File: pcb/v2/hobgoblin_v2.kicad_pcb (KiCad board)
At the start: 2 copper layers, 47 parts, among them J1 5V, J2 RC2014EXT1, J3 RC2014EXT2, SW1 RESET, SW2 ROMBNK, SW3 USBUART, U1 74LS32, U10 MC68B50, U2 74LS14, U3 Z80CPU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

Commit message: Start using GALs in V2
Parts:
- added REF**: M3, MountingHole:MountingHole_3.2mm_M3, F.Cu at (186.5, 33.5)
- added REF**: M3, MountingHole:MountingHole_3.2mm_M3, F.Cu at (33.5, 141.5)
- added REF**: M3, MountingHole:MountingHole_3.2mm_M3, F.Cu at (33.5, 33.5)
- added REF**: M3, MountingHole:MountingHole_3.2mm_M3, F.Cu at (186.5, 141.5)
- moved C10 168.4 mm to (269.3, 133.6)
- moved R10 168.4 mm to (256.0, 129.6)
- moved R5 168.4 mm to (256.0, 137.7)
- moved C11 168.4 mm to (286.4, 115.4)
- moved C7 168.4 mm to (256.0, 141.8)
- moved D1 168.4 mm to (280.8, 111.6)
- moved R11 168.4 mm to (256.0, 133.6)
- moved R2 168.4 mm to (273.0, 121.0)
- moved R4 168.4 mm to (292.5, 103.0)
- moved R8 168.4 mm to (292.5, 99.0)
- moved R9 168.4 mm to (273.0, 116.9)
- moved SW1 168.4 mm to (273.5, 125.0)
- moved U1 168.4 mm to (233.2, 136.4)
- moved U7 168.4 mm to (244.8, 126.6)
- moved U9 168.4 mm to (281.3, 84.8)
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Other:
- board outline added: 160 x 115 mm

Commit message: Draft component placement
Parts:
- added C14: 10uF, Capacitor_THT:CP_Radial_D4.0mm_P1.50mm, F.Cu at (101.2, 37.1)
- added C15: 0.1uF, Capacitor_THT:C_Disc_D3.8mm_W2.6mm_P2.50mm, F.Cu at (117.8, 39.8)
- added C16: 0.1uF, Capacitor_THT:C_Disc_D3.8mm_W2.6mm_P2.50mm, F.Cu at (41.8, 81.2)
- added J4: MINIUSB, Connector_USB:USB_Mini-B_Lumberg_2486_01_Horizontal, F.Cu at (162.2, 34.6)
- added JP1: USB_VCC, Connector_PinSocket_2.54mm:PinSocket_1x02_P2.54mm_Vertical, F.Cu at (163.7, 43.4)
- U4: value 74LS138 -> GAL16V8/IO; footprint Package_DIP:DIP-16_W7.62mm_LongPads -> Package_DIP:DIP-20_W7.62mm_Socket_LongPads
- U5: value 74LS32 -> FT232RL; footprint Package_DIP:DIP-14_W7.62mm_LongPads -> Package_SO:SSOP-28_5.3x10.2mm_P0.65mm
- U9: value GAL16V8 -> GAL16V8/MEM
- moved C8 211.1 mm to (56.8, 81.2), turned to 90 degrees
- moved D1 207.6 mm to (73.2, 109.5), turned to 180 degrees
- moved C1 206.0 mm to (60.5, 115.2)
- moved C13 195.0 mm to (68.0, 119.4)
- moved C3 188.0 mm to (66.9, 78.2), turned to 90 degrees
- moved R4 185.0 mm to (107.6, 101.5), turned to 180 degrees
- moved SW3 178.0 mm to (126.7, 43.6), turned to 90 degrees
- moved U2 177.6 mm to (65.4, 122.5)
- moved C4 169.7 mm to (84.5, 119.4)
- moved R8 161.9 mm to (130.7, 97.0)
- moved R3 160.0 mm to (81.1, 108.0)
- moved SW1 159.4 mm to (141.5, 35.8)
- moved R1 157.0 mm to (91.2, 111.2), turned to 180 degrees
- moved C2 154.4 mm to (106.3, 49.8)
- moved C5 152.9 mm to (101.0, 119.4)
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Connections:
- CF1 pad 7: /~{PORT10} -> /~{IO_CF}
- SW3 pad 4: /RX -> /USB_UART/RX
- SW3 pad 5: /~{RTS}_1 -> /USB_UART/~{RTS}
- SW3 pad 6: /TX -> /USB_UART/TX
- U10 pad 10: /A7 -> unconnected-(U10-Pad10)
- U10 pad 8: /~{M1} -> unconnected-(U10-Pad8)
- U10 pad 9: /A6 -> /~{IO_UART}
- U4 pad 1: /A3 -> /~{M1}
- U4 pad 10: unconnected-(U4-Pad10) -> GND
- U4 pad 11: unconnected-(U4-Pad11) -> /A10
- U4 pad 12: unconnected-(U4-Pad12) -> /A15
- U4 pad 13: /~{PORT10} -> /A14
- U4 pad 14: unconnected-(U4-Pad14) -> /~{ROM_OFF}
- U4 pad 15: unconnected-(U4-Pad15) -> /~{IO_CF}
- U4 pad 16: VCC -> /~{IO_UART}
- U4 pad 2: /A4 -> /~{IOWR}
- U4 pad 3: /A5 -> /A3
- U4 pad 4: /A7 -> /A4
- U4 pad 5: /A6 -> /A5
- U4 pad 6: /~{M1} -> /A6
- U4 pad 7: /~{PORT38} -> /A7
- U4 pad 8: GND -> /A8
- U4 pad 9: unconnected-(U4-Pad9) -> /A9
- U5 pad 1: /~{IOWR} -> /USB_UART/RX
- U5 pad 10: (no net) -> unconnected-(U5-Pad10)
- U5 pad 11: (no net) -> /USB_UART/~{RTS}
- U5 pad 12: (no net) -> unconnected-(U5-Pad12)
- U5 pad 13: (no net) -> unconnected-(U5-Pad13)
- U5 pad 14: VCC -> unconnected-(U5-Pad14)
- U5 pad 2: /~{PORT38} -> unconnected-(U5-Pad2)
- U5 pad 3: /~{ROMOFF} -> unconnected-(U5-Pad3)
- U5 pad 4: (no net) -> VCC
- U5 pad 5: (no net) -> /USB_UART/TX
- U5 pad 6: (no net) -> unconnected-(U5-Pad6)
- U5 pad 9: (no net) -> unconnected-(U5-Pad9)
- U7 pad 5: /~{ROMOFF} -> /~{ROM_OFF}

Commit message: Realign components
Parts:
- moved X2 15.6 mm to (72.2, 33.8)
- moved X1 15.0 mm to (55.7, 33.8)
- moved JP1 14.4 mm to (152.5, 34.3)
- moved C11 14.1 mm to (124.5, 101.8)
- moved C3 14.1 mm to (56.9, 68.2)
- moved C1 14.1 mm to (50.5, 105.2)
- moved C10 14.1 mm to (156.3, 39.8)
- moved C13 14.1 mm to (58.0, 109.4)
- moved C2 14.1 mm to (96.3, 39.8)
- moved C4 14.1 mm to (74.5, 109.4)
- moved C5 14.1 mm to (91.0, 109.4)
- moved C6 14.1 mm to (126.3, 40.0)
- moved C7 14.1 mm to (108.0, 101.8)
- moved C8 14.1 mm to (46.8, 71.2)
- moved C9 14.1 mm to (139.0, 103.2)
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
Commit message: CF socket properties
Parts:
- CF1: value CF_Socket -> CompactFlash
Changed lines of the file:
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@@
     (property "Sheetname" "")
     (attr smd)
-    (fp_text reference "CF1" (at 7.22 0 90) (layer "F.SilkS")
+    (fp_text reference "CF1" (at 7.22 0 90) (layer "F.SilkS") hide
       (effects (font (size 1 1) (thickness 0.15)))
     )
-    (fp_text value "CF_Socket" (at 10.39 0 90) (layer "F.Fab")
+    (fp_text value "CompactFlash" (at 10.39 0 90) (layer "F.SilkS")
       (effects (font (size 1 1) (thickness 0.15)))
     )

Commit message: Tweak silkscreen
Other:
- board text added: "Hobgoblin Computer v2.0 Ilya Strukov 2022"
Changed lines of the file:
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@@
       (effects (font (size 1 1) (thickness 0.15)))
     )
-    (fp_text value "CompactFlash" (at 10.39 0 90) (layer "F.SilkS")
+    (fp_text value "CompactFlash" (at 18 0 90) (layer "F.SilkS")
       (effects (font (size 1 1) (thickness 0.15)))
     )
@@
   (gr_arc (start 180 133) (mid 179.414214 134.414214) (end 178 135) (layer "Edge.Cuts") (width 0.1))
   (gr_arc (start 20 22) (mid 20.585786 20.585786) (end 22 20) (layer "Edge.Cuts") (width 0.1))
+  (gr_text "Hobgoblin Computer v2.0 Ilya Strukov 2022" (at 53.75 132.75) (layer "F.SilkS")
+    (effects (font (size 1.5 1.5) (thickness 0.2)))
+  )
 )

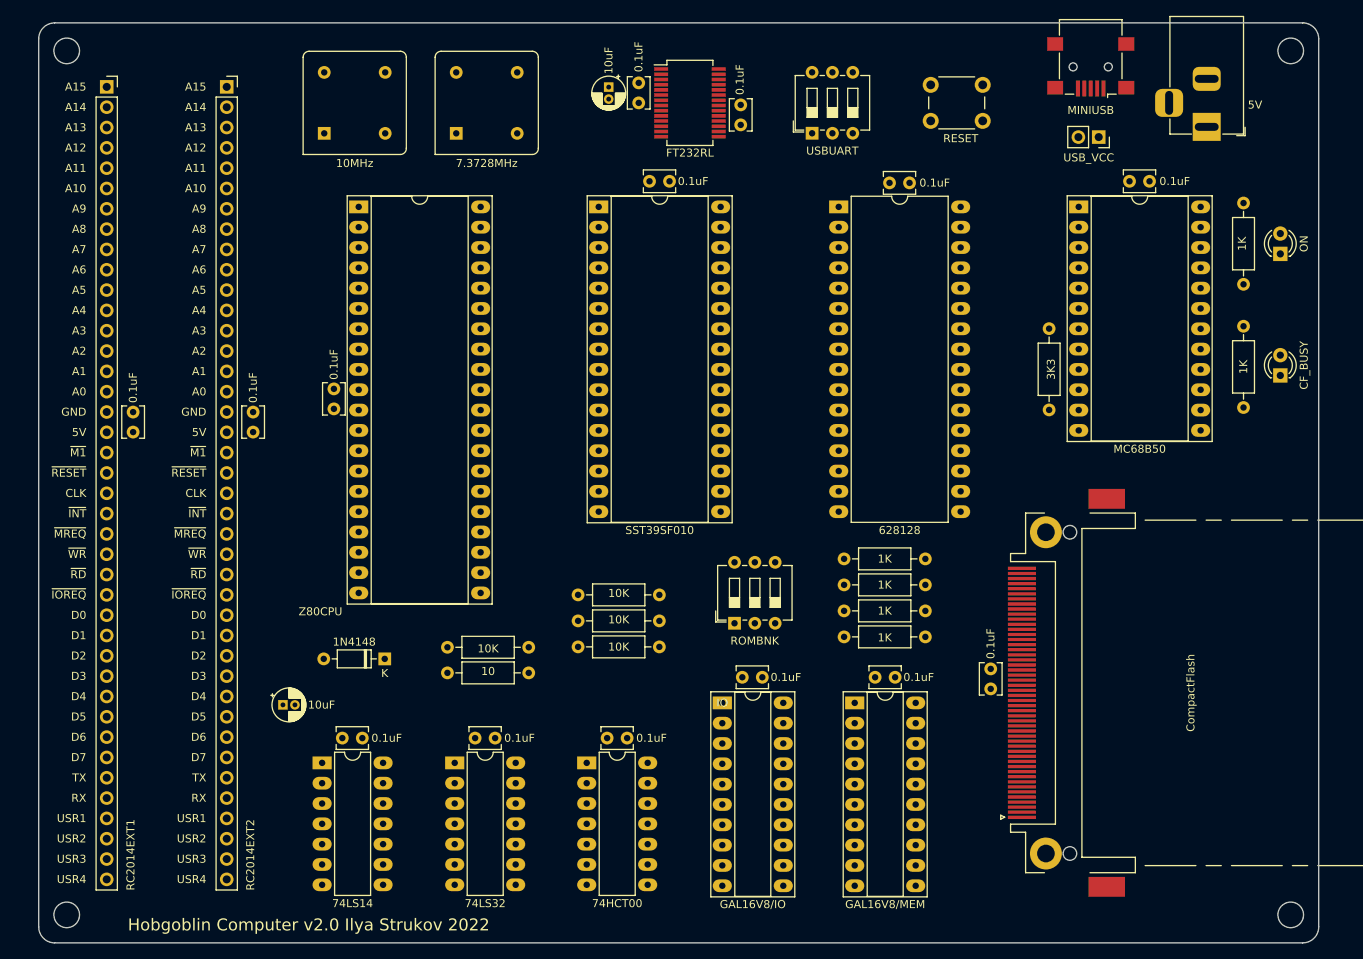
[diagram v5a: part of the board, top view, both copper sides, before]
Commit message: Add ground fills
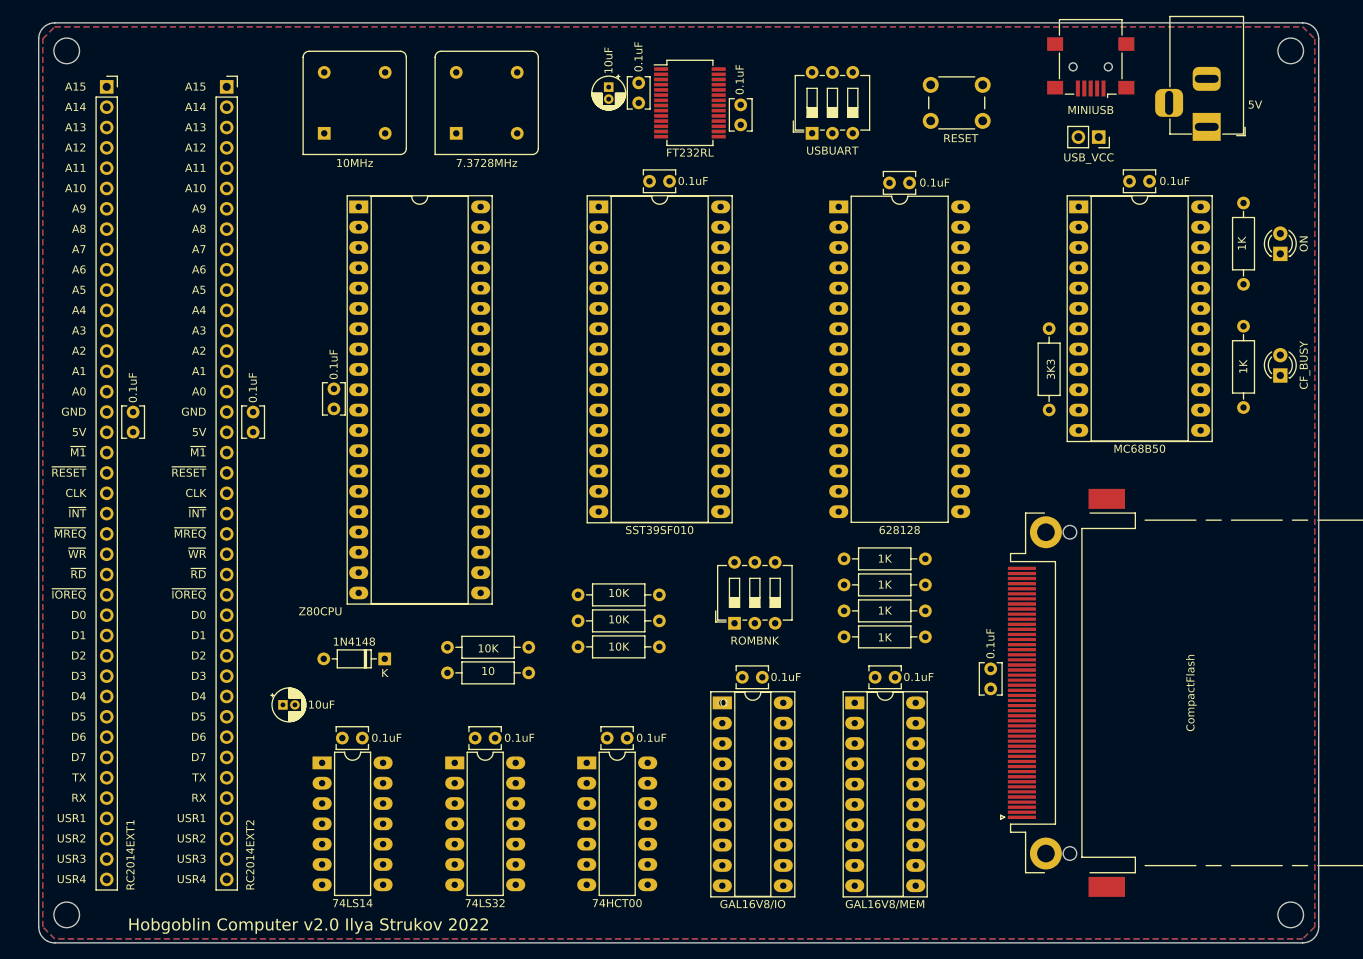
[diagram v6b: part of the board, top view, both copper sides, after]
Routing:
- added copper zone on B.Cu, net GND
- added copper zone on F.Cu, net GND
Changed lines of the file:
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@@
     (effects (font (size 1.5 1.5) (thickness 0.2)))
   )
+  (zone (net 2) (net_name "GND") (layers F&B.Cu) (hatch edge 0.508)
+    (connect_pads (clearance 0.508))
+    (min_thickness 0.254) (filled_areas_thickness no)
+    (fill yes (thermal_gap 0.508) (thermal_bridge_width 0.508))
+    (polygon
+      (pts
+        (xy 179.5 22)
+        (xy 179.5 133)
+        (xy 178 134.5)
+        (xy 22 134.5)
+        (xy 20.5 133)
+        (xy 20.5 22)
+        (xy 22 20.5)
+        (xy 178 20.5)
+      )
+    )
+  )
 )

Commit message: In-progress PCB layout
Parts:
- moved R2 71.1 mm to (81.3, 97.1), turned to 180 degrees
- moved U6 30.0 mm to (90.0, 43.0)
- moved U8 30.0 mm to (120.0, 43.0)
- moved C1 7.29 mm to (51.5, 112.5), turned to 90 degrees
- moved C11 2.50 mm to (127.0, 101.8), turned to 180 degrees
- moved C13 2.50 mm to (60.5, 109.4), turned to 180 degrees
- moved C2 2.50 mm to (98.8, 39.8), turned to 180 degrees
- moved C4 2.50 mm to (77.0, 109.4), turned to 180 degrees
- moved C5 2.50 mm to (93.5, 109.4), turned to 180 degrees
- moved C6 2.50 mm to (128.8, 40.0), turned to 180 degrees
- moved C7 2.50 mm to (110.5, 101.8), turned to 180 degrees
- moved R1 2.25 mm to (81.2, 103.5)
- moved R3 2.25 mm to (71.1, 100.3)
- moved C3 0.25 mm to (56.9, 68.5)
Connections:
- net Net-(J4-Pad1) renamed /USB_UART/USB_VCC
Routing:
- net VCC: track 0.00 -> 590.2 mm, vias 0 -> 11
- net /D2: track 0.00 -> 222.5 mm, vias 0 -> 3
- net /A14: track 0.00 -> 204.0 mm, vias 0 -> 4
- net /D1: track 0.00 -> 204.0 mm, vias 0 -> 2
- net /D4: track 0.00 -> 189.8 mm, vias 0 -> 2
- net /D3: track 0.00 -> 185.2 mm, vias 0 -> 2
- net /D0: track 0.00 -> 182.6 mm, vias 0 -> 3
- net /D5: track 0.00 -> 157.5 mm, vias 0 -> 3
- net /D7: track 0.00 -> 145.6 mm, vias 0 -> 2
- net /A11: track 0.00 -> 145.2 mm, vias 0 -> 2
- net /A13: track 0.00 -> 141.0 mm
- net /A10: track 0.00 -> 132.4 mm, vias 0 -> 2
- net /A15: track 0.00 -> 130.1 mm, vias 0 -> 2
- net /D6: track 0.00 -> 127.7 mm, vias 0 -> 4
- net /A0: track 0.00 -> 126.8 mm
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
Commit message: PCB layout in progress
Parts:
- removed REF** (x4): M3, MountingHole:MountingHole_3.2mm_M3
- removed SW3: USBUART, Button_Switch_THT:SW_DIP_SPSTx03_Slide_6.7x9.18mm_W7.62mm_P2.54mm_LowProfile
- added J5: USBUART, Connector_PinHeader_2.54mm:PinHeader_2x03_P2.54mm_Vertical, F.Cu at (131.0, 25.0)
- added REF1: hole1, MountingHole:MountingHole_3.2mm_M3_Pad, F.Cu at (24.0, 24.0)
- added REF1: hole3, MountingHole:MountingHole_3.2mm_M3_Pad, F.Cu at (24.0, 136.0)
- added REF1: hole4, MountingHole:MountingHole_3.2mm_M3_Pad, F.Cu at (176.0, 136.0)
- added REF1: hole2, MountingHole:MountingHole_3.2mm_M3_Pad, F.Cu at (176.0, 24.0)
- moved U10 112.7 mm to (54.9, 103.5)
- moved C8 102.0 mm to (147.0, 52.0), turned to 180 degrees
- moved C4 99.8 mm to (151.8, 43.2), turned to 90 degrees
- moved C6 87.8 mm to (48.0, 74.2), turned to 90 degrees
- moved R6 76.1 mm to (85.0, 22.9), turned to -90 degrees
- moved R12 75.6 mm to (129.0, 121.0)
- moved D3 73.8 mm to (135.0, 126.0), turned to 180 degrees
- moved R5 73.5 mm to (82.0, 22.9), turned to -90 degrees
- moved X2 73.3 mm to (103.7, 100.0)
- moved SW2 71.4 mm to (100.0, 24.0), turned to -90 degrees
- moved R4 71.1 mm to (79.0, 22.9), turned to -90 degrees
- moved C5 69.8 mm to (33.2, 74.2), turned to 90 degrees
- moved C16 68.6 mm to (91.2, 37.0), turned to 180 degrees
- moved C14 65.9 mm to (155.5, 42.7), turned to 90 degrees
- moved U9 64.0 mm to (162.0, 55.0)
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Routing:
- net VCC: track 590.2 -> 68.0 mm, vias 11 -> 0
- net /ROM_A15: track 0.00 -> 141.2 mm, vias 0 -> 3
- net /D2: track 222.5 -> 95.4 mm, vias 3 -> 4
- net /~{ROM}: track 0.00 -> 102.0 mm, vias 0 -> 2
- net /ROM_A14: track 0.00 -> 94.9 mm, vias 0 -> 2
- net /A15: track 130.1 -> 222.9 mm, vias 2 -> 6
- net /D1: track 204.0 -> 135.1 mm, vias 2 -> 3
- net /D0: track 182.6 -> 119.7 mm, vias 3 -> 2
- net /A12: track 120.2 -> 174.8 mm, vias 0 -> 4
- net /A10: track 132.4 -> 184.9 mm, vias 2 -> 4
- net /~{RAM}: track 0.00 -> 51.1 mm, vias 0 -> 2
- net /D5: track 157.5 -> 204.6 mm, vias 3 -> 5
- net /A0: track 126.8 -> 169.7 mm, vias 0 -> 2
- net /A7: track 94.4 -> 136.5 mm, vias 0 -> 2
- net /D7: track 145.6 -> 186.0 mm, vias 2 -> 3
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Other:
- board size 160 x 115 mm -> 160 x 120 mm
- board text removed: "Hobgoblin Computer v2.0 Ilya Strukov 2022"
